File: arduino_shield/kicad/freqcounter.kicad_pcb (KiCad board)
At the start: 2 copper layers, 47 x 53.3 mm, 34 parts, among them J1 ICSP PICKIT, J10 INPUT_A, J11 INPUT_B, J12 INPUT_ZCD, J13 I2C_1, J14 I2C_2, J15 PARALEL, J16 Ext_Clk, J2 Arduino_Power, J3 Arduino_Power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

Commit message: Updated Arduino-Shield Schematic and PCB
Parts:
- C4: value 100nF -> 1nF
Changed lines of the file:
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@@
   )
   (setup
-    (last_trace_width 1.016)
+    (last_trace_width 0.25)
     (user_trace_width 0.381)
     (user_trace_width 0.508)
@@
       (effects (font (size 1 1) (thickness 0.15)))
     )
-    (fp_text value 100nF (at 0 1.65 90) (layer F.Fab)
+    (fp_text value 1nF (at 0.245 -1.905 90) (layer F.Fab)
       (effects (font (size 1 1) (thickness 0.15)))
     )
@@
   (segment (start 150.625 93.885) (end 150.625 94.235) (width 0.508) (layer F.Cu) (net 1))
   (segment (start 150.625 94.085) (end 150.625 93.885) (width 1.016) (layer F.Cu) (net 1))
+  (segment (start 150.625 97.535) (end 150.075 96.985) (width 0.508) (layer F.Cu) (net 1))
+  (segment (start 150.625 97.885) (end 150.625 97.535) (width 0.508) (layer F.Cu) (net 1))
+  (segment (start 150.25 98.26) (end 150.625 97.885) (width 1.016) (layer F.Cu) (net 1))
+  (segment (start 150.25 100.33) (end 150.25 98.26) (width 1.016) (layer F.Cu) (net 1))
+  (segment (start 150.625 97.885) (end 150.625 93.885) (width 1.016) (layer F.Cu) (net 1))
+  (segment (start 150.625 90.935) (end 149.86 90.17) (width 1.016) (layer F.Cu) (net 1))
+  (segment (start 150.625 93.885) (end 150.625 90.935) (width 1.016) (layer F.Cu) (net 1))
+  (segment (start 150.25 100.33) (end 150.25 101.21) (width 1.016) (layer F.Cu) (net 1))
+  (segment (start 150.25 101.21) (end 149.86 101.6) (width 1.016) (layer F.Cu) (net 1))
+  (via (at 149.86 101.6) (size 0.8) (drill 0.4) (layers F.Cu B.Cu) (net 1))
+  (via (at 151.002992 101.6) (size 0.8) (drill 0.4) (layers F.Cu B.Cu) (net 1))
+  (segment (start 151.002992 101.082992) (end 151.002992 101.6) (width 1.016) (layer F.Cu) (net 1))
+  (segment (start 150.25 100.33) (end 151.002992 101.082992) (width 1.016) (layer F.Cu) (net 1))
+  (segment (start 149.460001 101.999999) (end 149.86 101.6) (width 1.016) (layer F.Cu) (net 1))
+  (segment (start 148.64399 102.81601) (end 149.460001 101.999999) (width 1.016) (layer F.Cu) (net 1))
+  (segment (start 144.83399 102.81601) (end 148.64399 102.81601) (width 1.016) (layer F.Cu) (net 1))
+  (segment (start 142.24 105.41) (end 144.83399 102.81601) (width 1.016) (layer F.Cu) (net 1))
+  (segment (start 149.86 101.6) (end 151.002992 101.6) (width 1.016) (layer F.Cu) (net 1))
   (segment (start 147.701 81.28) (end 149.225 81.28) (width 0.508) (layer F.Cu) (net 2))
   (segment (start 146.429378 81.28) (end 147.701 81.28) (width 0.508) (layer F.Cu) (net 2))
@@
   (segment (start 143.510022 72.135978) (end 143.002 72.644) (width 1.016) (layer F.Cu) (net 8))
   (segment (start 143.510022 71.754996) (end 143.510022 72.135978) (width 1.016) (layer F.Cu) (net 8))
+  (segment (start 145.415 85.725) (end 147.32 87.63) (width 0.508) (layer F.Cu) (net 9))
+  (segment (start 143.13 85.725) (end 145.415 85.725) (width 0.508) (layer F.Cu) (net 9))
+  (segment (start 147.32 87.63) (end 149.86 87.63) (width 0.508) (layer F.Cu) (net 9))
   (segment (start 145.825 95.885) (end 147.825 93.885) (width 0.508) (layer F.Cu) (net 10))
   (segment (start 145.415 95.885) (end 145.825 95.885) (width 0.508) (layer F.Cu) (net 10))
@@
   (segment (start 145.025 78.105) (end 146.685 79.765) (width 0.508) (layer F.Cu) (net 43))
   (segment (start 143.13 78.105) (end 145.025 78.105) (width 0.508) (layer F.Cu) (net 43))
-  (segment (start 150.625 97.535) (end 150.075 96.985) (width 0.508) (layer F.Cu) (net 1))
-  (segment (start 150.625 97.885) (end 150.625 97.535) (width 0.508) (layer F.Cu) (net 1))
-  (segment (start 150.25 98.26) (end 150.625 97.885) (width 1.016) (layer F.Cu) (net 1))
-  (segment (start 150.25 100.33) (end 150.25 98.26) (width 1.016) (layer F.Cu) (net 1))
-  (segment (start 150.625 97.885) (end 150.625 93.885) (width 1.016) (layer F.Cu) (net 1))
-  (segment (start 150.625 90.935) (end 149.86 90.17) (width 1.016) (layer F.Cu) (net 1))
-  (segment (start 150.625 93.885) (end 150.625 90.935) (width 1.016) (layer F.Cu) (net 1))
-  (segment (start 150.25 100.33) (end 150.25 101.21) (width 1.016) (layer F.Cu) (net 1))
-  (segment (start 150.25 101.21) (end 149.86 101.6) (width 1.016) (layer F.Cu) (net 1))
-  (via (at 149.86 101.6) (size 0.8) (drill 0.4) (layers F.Cu B.Cu) (net 1))
-  (via (at 151.002992 101.6) (size 0.8) (drill 0.4) (layers F.Cu B.Cu) (net 1))
-  (segment (start 151.002992 101.082992) (end 151.002992 101.6) (width 1.016) (layer F.Cu) (net 1))
-  (segment (start 150.25 100.33) (end 151.002992 101.082992) (width 1.016) (layer F.Cu) (net 1))
-  (segment (start 149.460001 101.999999) (end 149.86 101.6) (width 1.016) (layer F.Cu) (net 1))
-  (segment (start 148.64399 102.81601) (end 149.460001 101.999999) (width 1.016) (layer F.Cu) (net 1))
-  (segment (start 144.83399 102.81601) (end 148.64399 102.81601) (width 1.016) (layer F.Cu) (net 1))
-  (segment (start 142.24 105.41) (end 144.83399 102.81601) (width 1.016) (layer F.Cu) (net 1))
-  (segment (start 149.86 101.6) (end 151.002992 101.6) (width 1.016) (layer F.Cu) (net 1))
-  (segment (start 145.415 85.725) (end 147.32 87.63) (width 0.508) (layer F.Cu) (net 9))
-  (segment (start 143.13 85.725) (end 145.415 85.725) (width 0.508) (layer F.Cu) (net 9))
-  (segment (start 147.32 87.63) (end 149.86 87.63) (width 0.508) (layer F.Cu) (net 9))
   (segment (start 133.73 75.565) (end 133.35 75.565) (width 0.508) (layer F.Cu) (net 45))
   (segment (start 133.35 75.565) (end 132.715 74.93) (width 0.508) (layer F.Cu) (net 45))

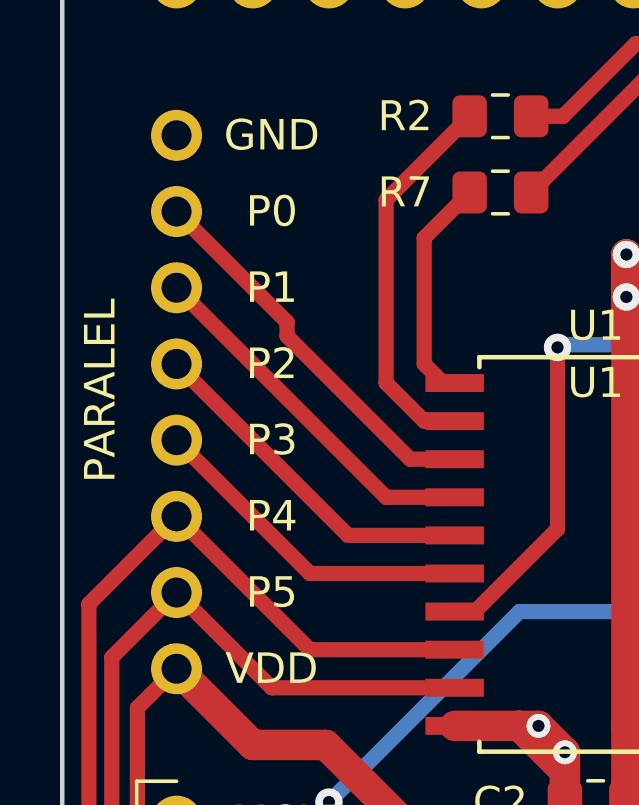
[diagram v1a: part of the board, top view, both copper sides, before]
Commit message: Updated schematic and PCB with LCD connector
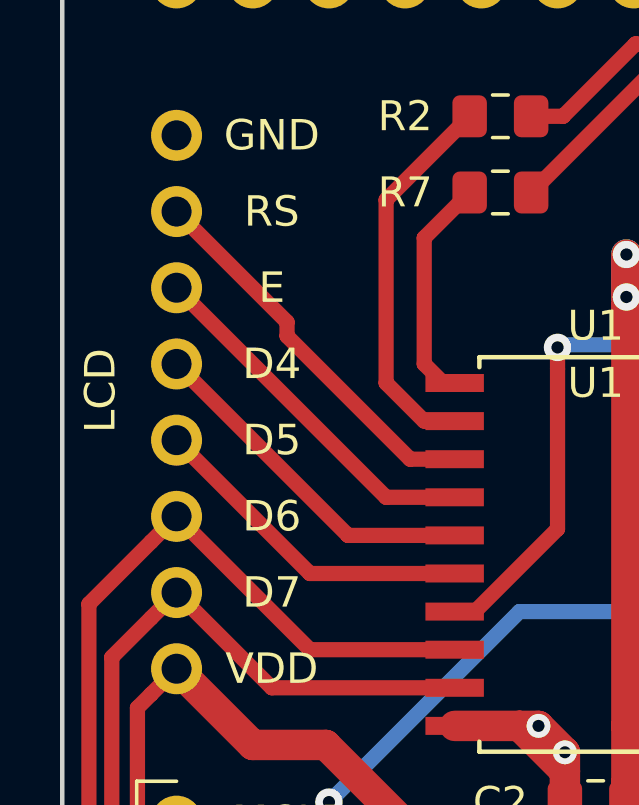
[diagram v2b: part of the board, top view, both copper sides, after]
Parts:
- J15: value PARALEL -> LCD
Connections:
- net ICSPCLK renamed D6
- net ICSPDAT renamed D7
- J15 pad 4: P3 -> D5
- J15 pad 5: P2 -> D4
- J15 pad 6: P1 -> E
- J15 pad 7: P0 -> RS
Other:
- board text added: "D4"
- board text added: "D5"
- board text added: "D6"
- board text added: "D7"
- board text added: "E"
- board text added: "RS"
- board text removed: "P0"
- board text removed: "P1"
- board text removed: "P2"
- board text removed: "P3"
- board text removed: "P4"
- board text removed: "P5"
